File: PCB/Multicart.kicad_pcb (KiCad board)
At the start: 2 copper layers, 78 x 87.5 mm, 45 parts, among them J1 DB25_Plug, SW1 RST, SW2 NEXT, U1 DS1812, U2 74HC00, U3 LM810, U4 AT89C2051-12P, U5 SST39SF040, U6 SST39SF040, U7 SST39SF040, U8 SA39-12SRWA, U9 74LS573, Y1 12MHz

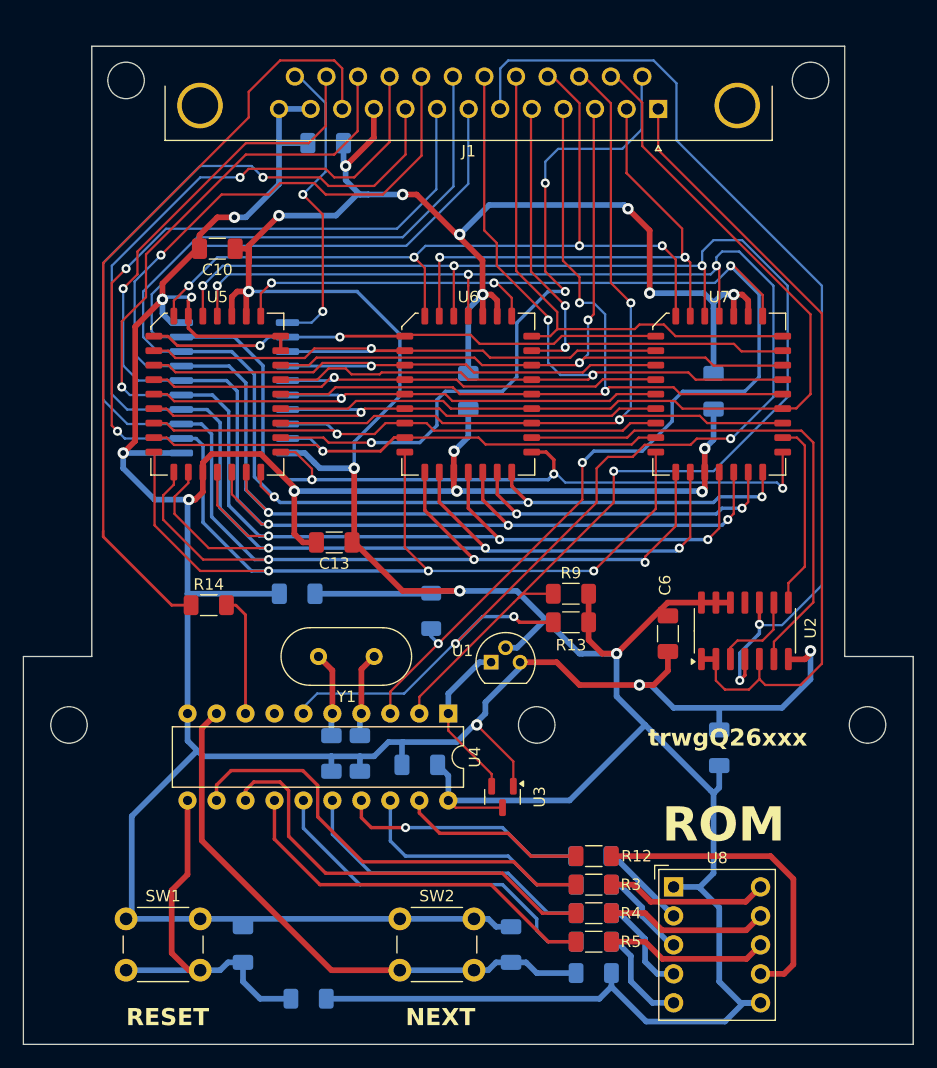
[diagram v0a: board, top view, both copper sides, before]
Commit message: PCB updated, B will be the last revision to use 89C2051
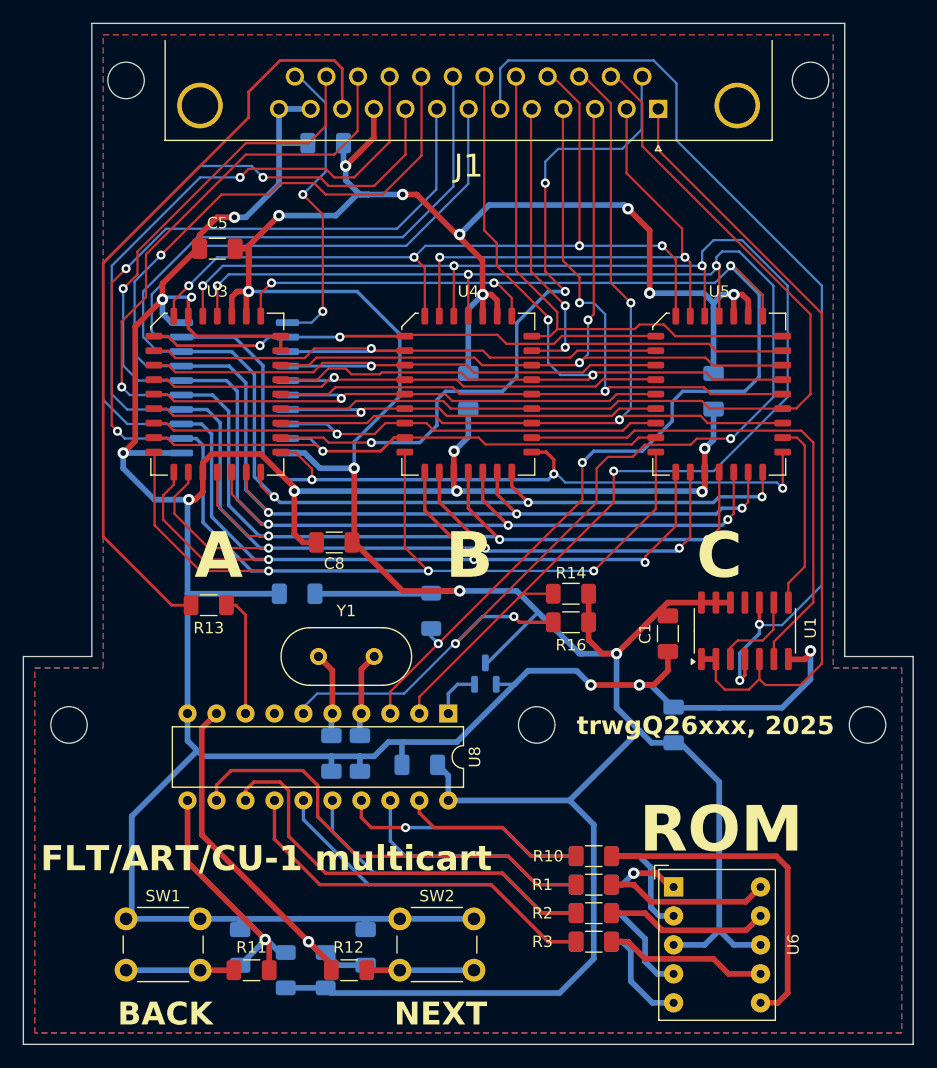
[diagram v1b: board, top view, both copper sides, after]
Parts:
- removed the U8 at (173.0, 96.2)
- removed U9: 74LS573, Package_SO:SOIC-20W_7.5x12.8mm_P1.27mm
- added R11: 330, Resistor_SMD:R_1206_3216Metric_Pad1.30x1.75mm_HandSolder, F.Cu at (136.0, 103.5)
- added R12: 330, Resistor_SMD:R_1206_3216Metric_Pad1.30x1.75mm_HandSolder, F.Cu at (144.6, 103.5)
- added U2: 74LS573, Package_SO:SOIC-20W_7.5x12.8mm_P1.27mm, B.Cu at (134.5, 52.4)
- H1, H2, H3, H4, H5: renamed from REF**; value M3 -> ~
- J1: value DB25_Plug -> MODULE
- SW1: value RST -> BACK
- U6: renamed from U1; value DS1812 -> SA39-11SRWA; footprint Package_TO_SOT_THT:TO-92 -> Display_7Segment:Sx39-1xxxxx
- U7: renamed from U3; value LM810 -> MAX810; moved to B.Cu
- Y1: value 12MHz -> 3.6864MHz
- moved U6 25.4 mm to (173.0, 96.2)
- moved R7 23.5 mm to (142.5, 103.5), turned to -90 degrees
- moved C13 12.8 mm to (146.0, 101.5)
- moved U7 10.9 mm to (156.5, 77.5), turned to 90 degrees
- moved C4 4.47 mm to (173.0, 82.0)
- moved R6 3.20 mm to (139.0, 103.5), turned to -90 degrees
- moved C12 0.35 mm to (135.0, 101.5)
- moved R8 0.05 mm to (166.0, 93.5)
- renumbered C6 to C1, C8 to C10, C9 to C11, C1 to C12, C4 to C13, C5 to C4, C10 to C5, C11 to C6, C12 to C7, C13 to C8, C7 to C9, R3 to R1, R12 to R10, R14 to R13, R9 to R14, R11 to R15, R13 to R16, R4 to R2, R5 to R3, R6 to R4, R7 to R5, R1 to R6, R2 to R7, R10 to R9, U2 to U1, U5 to U3, U6 to U4, U7 to U5, U4 to U8
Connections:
- C12 pad 1: RST_SW -> BACK_SW
- J1 pad 0: (no net) -> GND
- R1 pad 2: Net-(U8-A) -> Net-(U6-A)
- R10 pad 2: Net-(U8-DP) -> Net-(U6-DP)
- R2 pad 2: Net-(U8-B) -> Net-(U6-B)
- R3 pad 2: Net-(U8-C) -> Net-(U6-C)
- R4 pad 2: Net-(U8-D) -> Net-(U6-D)
- R5 pad 2: Net-(U8-E) -> Net-(U6-E)
- R6 pad 1: RST_SW -> BACK_SW
- R8 pad 2: Net-(U8-F) -> Net-(U6-F)
- R9 pad 2: Net-(U8-G) -> Net-(U6-G)
- SW1 pad 2: RST_SW -> Net-(R11-Pad2)
- SW2 pad 2: NEXT_SW -> Net-(R12-Pad2)
- U6 pad 1: CPU_RST -> Net-(U6-G)
- U6 pad 2: +5V -> Net-(U6-F)
- U6 pad 3: GND -> +5V
- U8 pad 11: RST_SW -> BACK_SW
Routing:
- net RST_SW: track 33.6 -> 0.00 mm
- net Net-(U6-DP): track 0.00 -> 29.6 mm
- net Net-(U8-DP): track 27.5 -> 0.00 mm
- net BACK_SW: track 0.00 -> 22.9 mm, vias 0 -> 1
- net NEXT_SW: track 50.0 -> 33.7 mm, vias 0 -> 1
- net Net-(U6-C): track 0.00 -> 14.2 mm
- net Net-(U8-A): track 14.2 -> 0.00 mm
- net Net-(U6-A): track 0.00 -> 14.2 mm
- net Net-(U8-B): track 14.2 -> 0.00 mm
- net Net-(U6-B): track 0.00 -> 14.2 mm
- net Net-(U8-C): track 14.2 -> 0.00 mm
- net GND: track 311.2 -> 300.8 mm
- net CPU_RST: track 14.6 -> 4.39 mm
- net Net-(U6-F): track 0.00 -> 9.72 mm
- net Net-(R11-Pad2): track 0.00 -> 9.45 mm
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- added copper zone on B.Cu, net GND
- added copper zone on F.Cu, net GND
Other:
- board size 78 x 87.5 mm -> 78 x 89.5 mm
- board text added: "A"
- board text added: "B"
- board text added: "BACK"
- board text added: "C"
- board text added: "FLT/ART/CU-1 multicart"
- board text added: "trwgQ26xxx, 2025"
- board text removed: "RESET"
- board text removed: "trwgQ26xxx"

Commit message: Update for production
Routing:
- net +5V: track 319.2 -> 317.9 mm
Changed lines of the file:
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@@
 		(pad "1" thru_hole rect
 			(at 0 0)
-			(size 1.7 1.7)
+			(size 1.3 1.3)
 			(drill 0.7)
 			(layers "*.Cu" "*.Mask")
@@
 		(pad "2" thru_hole circle
 			(at 0 2.54)
-			(size 1.7 1.7)
+			(size 1.3 1.3)
 			(drill 0.7)
 			(layers "*.Cu" "*.Mask")
@@
 		(pad "3" thru_hole circle
 			(at 0 5.08)
-			(size 1.7 1.7)
+			(size 1.3 1.3)
 			(drill 0.7)
 			(layers "*.Cu" "*.Mask")
@@
 		(pad "4" thru_hole circle
 			(at 0 7.62)
-			(size 1.7 1.7)
+			(size 1.3 1.3)
 			(drill 0.7)
 			(layers "*.Cu" "*.Mask")
@@
 		(pad "5" thru_hole circle
 			(at 0 10.16)
-			(size 1.7 1.7)
+			(size 1.3 1.3)
 			(drill 0.7)
 			(layers "*.Cu" "*.Mask")
@@
 		(pad "6" thru_hole circle
 			(at 7.62 10.16)
-			(size 1.7 1.7)
+			(size 1.3 1.3)
 			(drill 0.7)
 			(layers "*.Cu" "*.Mask")
@@
 		(pad "7" thru_hole circle
 			(at 7.62 7.62)
-			(size 1.7 1.7)
+			(size 1.3 1.3)
 			(drill 0.7)
 			(layers "*.Cu" "*.Mask")
@@
 		(pad "8" thru_hole circle
 			(at 7.62 5.08)
-			(size 1.7 1.7)
+			(size 1.3 1.3)
 			(drill 0.7)
 			(layers "*.Cu" "*.Mask")
@@
 		(pad "9" thru_hole circle
 			(at 7.62 2.54)
-			(size 1.7 1.7)
+			(size 1.3 1.3)
 			(drill 0.7)
 			(layers "*.Cu" "*.Mask")
@@
 		(pad "10" thru_hole circle
 			(at 7.62 0)
-			(size 1.7 1.7)
+			(size 1.3 1.3)
 			(drill 0.7)
 			(layers "*.Cu" "*.Mask")
@@
 	)
 	(segment
-		(start 168 75.75)
-		(end 166.75 75.75)
-		(width 0.5)
-		(layer "F.Cu")
-		(net 4)
-	)
-	(segment
 		(start 134.27 46.1625)
 		(end 134.27 44.48)
@@
 	)
 	(segment
+		(start 171.875 71.875)
+		(end 169.75 74)
+		(width 0.5)
+		(layer "F.Cu")
+		(net 4)
+	)
+	(segment
 		(start 135.75 44)
 		(end 135.75 41.5)
@@
 	)
 	(segment
+		(start 167 73)
+		(end 165.55 73)
+		(width 0.5)
+		(layer "F.Cu")
+		(net 4)
+	)
+	(segment
 		(start 146.72 28)
 		(end 146.72 30.53)
@@
 	)
 	(segment
-		(start 134.27 44.48)
-		(end 134.75 44)
+		(start 168 74)
+		(end 167 73)
 		(width 0.5)
 		(layer "F.Cu")
@@
 	)
 	(segment
-		(start 171.875 71.875)
-		(end 168 75.75)
+		(start 134.27 44.48)
+		(end 134.75 44)
 		(width 0.5)
 		(layer "F.Cu")
@@
 	)
 	(segment
-		(start 166.75 75.75)
-		(end 165.55 74.55)
-		(width 0.5)
-		(layer "F.Cu")
-		(net 4)
-	)
-	(segment
 		(start 172.475 71.275)
 		(end 171.875 71.875)
@@
 	)
 	(segment
-		(start 165.55 74.55)
-		(end 165.55 73)
-		(width 0.5)
-		(layer "F.Cu")
-		(net 4)
-	)
-	(segment
 		(start 170.9 44.15)
 		(end 170.9 38.65)
@@
 	)
 	(segment
+		(start 169.75 74)
+		(end 168 74)
+		(width 0.5)
+		(layer "F.Cu")
+		(net 4)
+	)
+	(segment
 		(start 178.25 44.25)
 		(end 178.27 44.27)
@@
 	)
 	(via
-		(at 168 75.75)
+		(at 168 74)
 		(size 1)
 		(drill 0.5)
@@
 	)
 	(segment
-		(start 161.5 72.5)
-		(end 161.75 72.75)
-		(width 0.5)
-		(layer "B.Cu")
-		(net 4)
-	)
-	(segment
-		(start 168 80.5)
-		(end 170 82.5)
-		(width 0.5)
-		(layer "B.Cu")
-		(net 4)
-	)
-	(segment
 		(start 154.25 70.25)
 		(end 159.25 70.25)
@@
 	)
 	(segment
-		(start 165 75.75)
-		(end 168 75.75)
-		(width 0.5)
-		(layer "B.Cu")
-		(net 4)
-	)
-	(segment
 		(start 142.5 105.05)
 		(end 142.95 105.5)
@@
 	)
 	(segment
+		(start 168 74)
+		(end 163 74)
+		(width 0.5)
+		(layer "B.Cu")
+		(net 4)
+	)
+	(segment
 		(start 145.25 44)
 		(end 135.75 44)
@@
 	)
 	(segment
-		(start 168 75.75)
+		(start 168 74)
 		(end 168 80.5)
 		(width 0.5)
@@
 	)
 	(segment
+		(start 163 74)
+		(end 161.5 72.5)
+		(width 0.5)
+		(layer "B.Cu")
+		(net 4)
+	)
+	(segment
 		(start 144.0625 31)
 		(end 144.0625 32.8125)
@@
 	)
 	(segment
-		(start 164.75 75.75)
-		(end 165 75.75)
-		(width 0.5)
-		(layer "B.Cu")
-		(net 4)
-	)
-	(segment
 		(start 161 72.25)
 		(end 161.25 72.25)
@@
 	)
 	(segment
-		(start 161.75 72.75)
-		(end 164.75 75.75)
-		(width 0.5)
-		(layer "B.Cu")
-		(net 4)
-	)
-	(segment
 		(start 155 45.54)
 		(end 156.27 44.27)
@@
 		(width 0.5)
 		(layer "B.Cu")
+		(net 4)
+	)
+	(segment
+		(start 168 80.5)
+		(end 170 82.5)
+		(width 0.5)
+		(layer "B.Cu")
